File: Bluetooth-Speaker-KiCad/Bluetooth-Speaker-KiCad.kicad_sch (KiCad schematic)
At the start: 0 parts

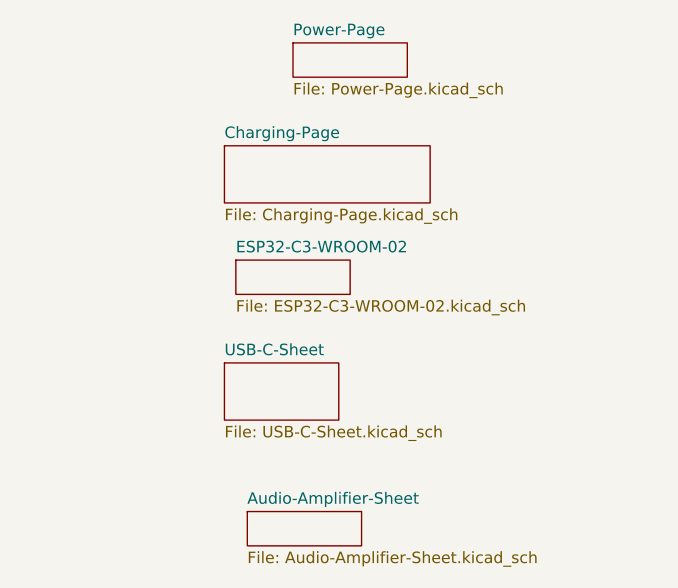
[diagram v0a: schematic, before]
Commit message: USB Connections
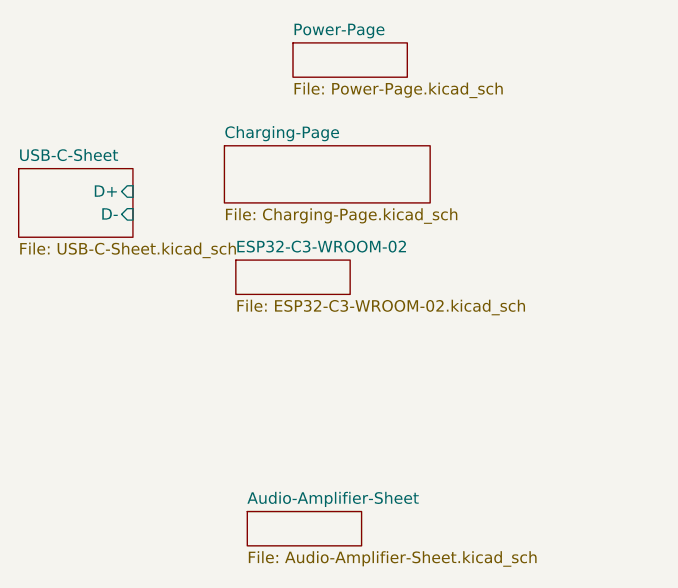
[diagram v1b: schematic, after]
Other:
- sheet USB-C-Sheet ports: added D+, D-; removed none
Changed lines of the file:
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@@
 	)
 	(sheet
-		(at 60.96 72.39)
-		(size 12.7 6.35)
+		(at 38.1 50.8)
+		(size 12.7 7.62)
 		(fields_autoplaced yes)
 		(stroke
@@
 		)
 		(property "Sheetname" "USB-C-Sheet"
-			(at 60.96 71.6784 0)
+			(at 38.1 50.0884 0)
 			(effects
 				(font
@@
 		)
 		(property "Sheetfile" "USB-C-Sheet.kicad_sch"
-			(at 60.96 79.3246 0)
+			(at 38.1 59.0046 0)
 			(effects
 				(font
@@
 			)
 		)
+		(pin "D-" input
+			(at 50.8 55.88 0)
+			(effects
+				(font
+					(size 1.27 1.27)
+				)
+				(justify right)
+			)
+		)
+		(pin "D+" input
+			(at 50.8 53.34 0)
+			(effects
+				(font
+					(size 1.27 1.27)
+				)
+				(justify right)
+			)
+		)

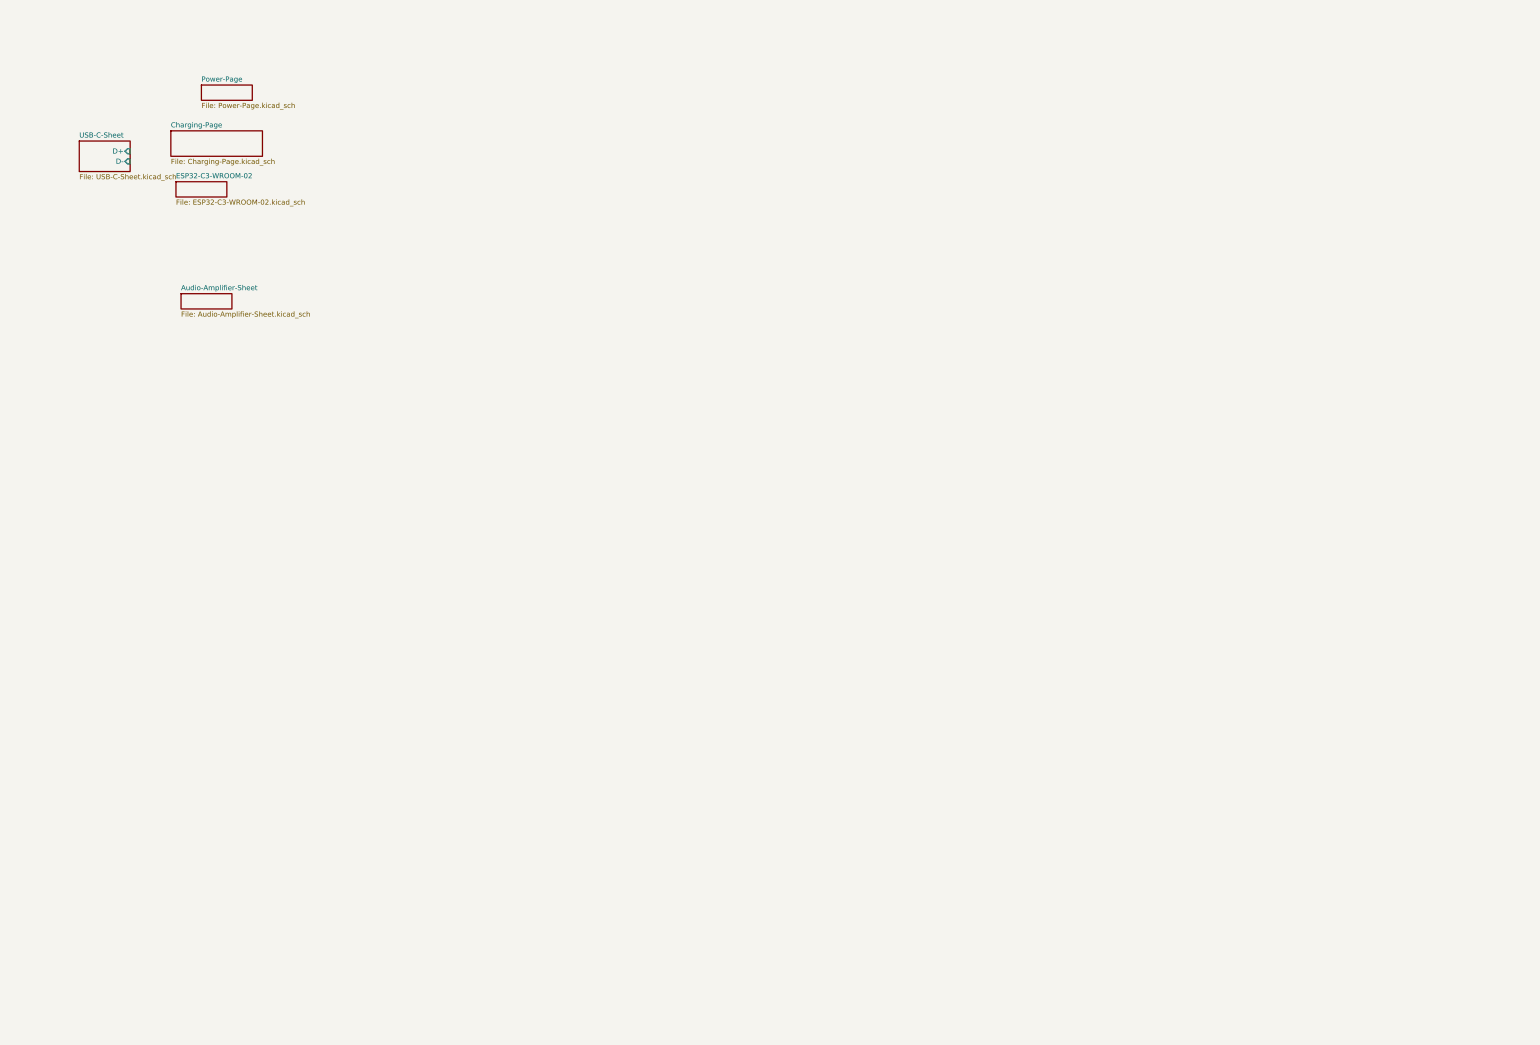
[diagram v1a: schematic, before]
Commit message: Updated battery charging
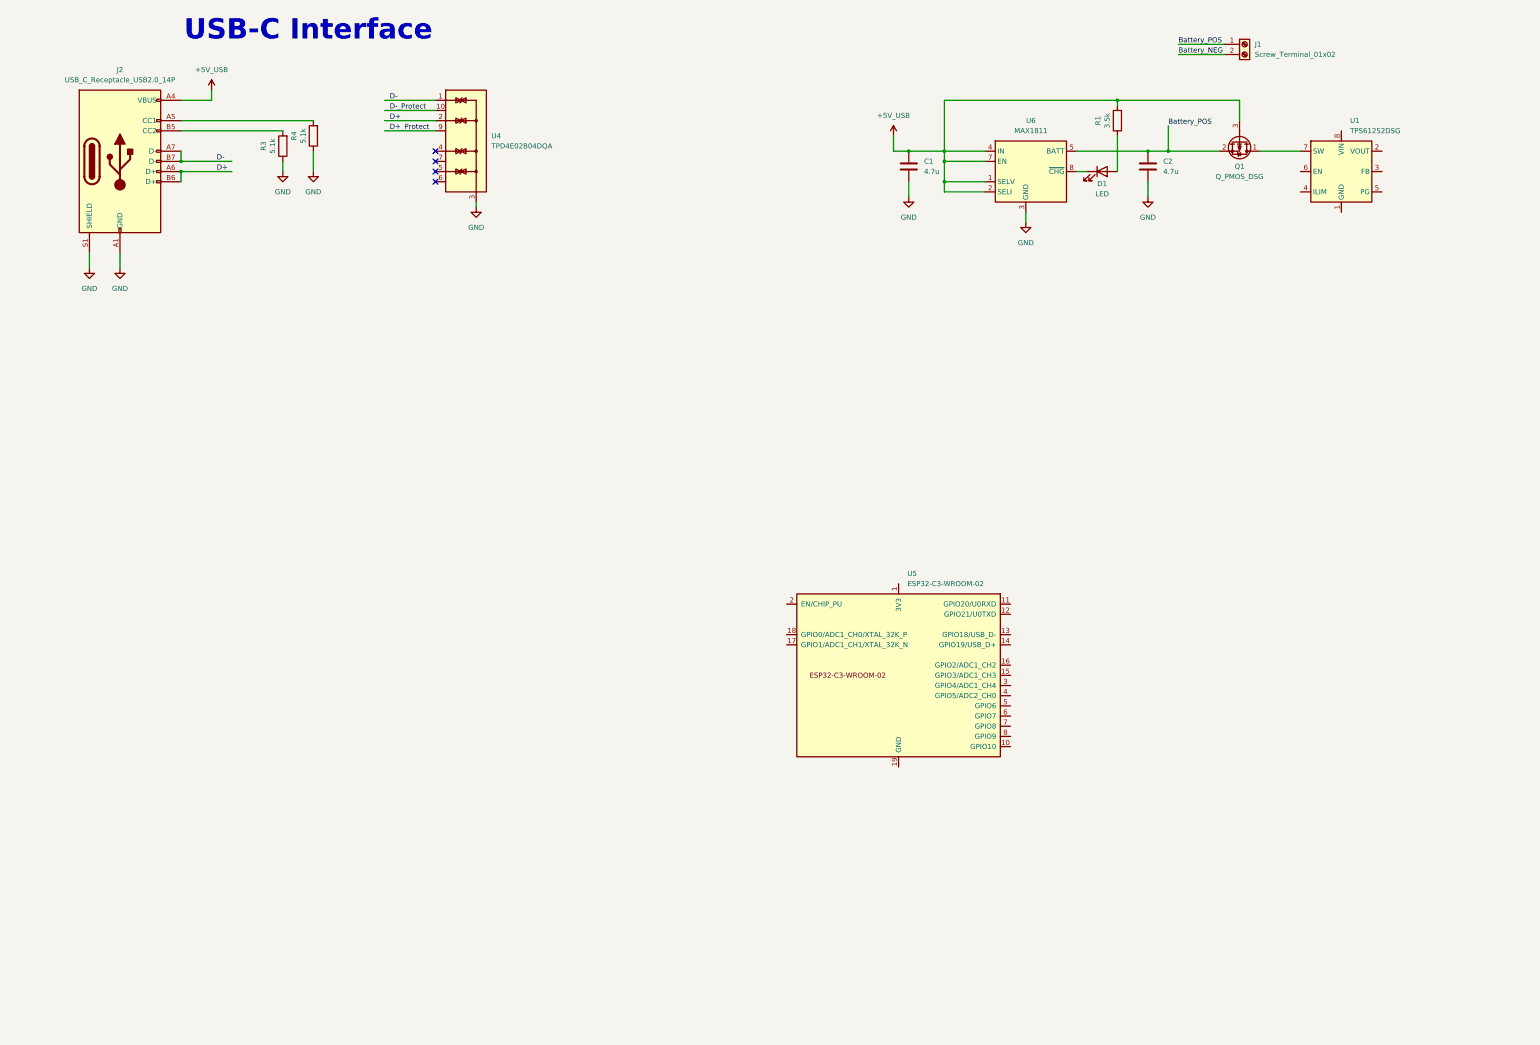
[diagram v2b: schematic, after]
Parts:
- added C1, C2: 4.7u, Capacitor_SMD:C_0603_1608Metric_Pad1.08x0.95mm_HandSolder, symbol Device:C
- added D1: LED, LED_SMD:LED_0603_1608Metric_Pad1.05x0.95mm_HandSolder, symbol Device:LED
- added J1: Screw_Terminal_01x02, symbol Connector:Screw_Terminal_01x02
- added J2: USB_C_Receptacle_USB2.0_14P, symbol Connector:USB_C_Receptacle_USB2.0_14P
- added Q1: Q_PMOS_DSG, symbol Device:Q_PMOS_DSG
- added R1: 3.5k, Resistor_SMD:R_0603_1608Metric_Pad0.98x0.95mm_HandSolder, symbol Device:R
- added R3, R4: 5.1k, Resistor_SMD:R_0603_1608Metric_Pad0.98x0.95mm_HandSolder, symbol Device:R
- added U1: TPS61252DSG, Package_SON:WSON-8-1EP_2x2mm_P0.5mm_EP0.9x1.6mm, symbol Regulator_Switching:TPS61252DSG
- added U4: TPD4E02B04DQA, Package_SON:USON-10_2.5x1.0mm_P0.5mm, symbol Power_Protection:TPD4E02B04DQA
- added U5: ESP32-C3-WROOM-02, PCM_Espressif:ESP32-C3-WROOM-02, symbol PCM_Espressif:ESP32-C3-WROOM-02
- added U6: MAX1811, Package_SO:SOIC-8_3.9x4.9mm_P1.27mm, symbol Battery_Management:MAX1811
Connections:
- new net: D1.1 (K), U6.8 (~{CHG})
- new net: J2.A5 (CC1), R4.2
- new net: U1.1 (GND), U1.9 (GND)
- new net: Q1.1 (D), U1.7 (SW)
- new net: D1.2 (A), R1.1
- new net: J2.B5 (CC2), R3.2
- new net: U5.19 (GND), U5.9 (GND)
- new net +5V_USB: C1.1, J2.A4 (VBUS), J2.A9 (VBUS), J2.B4 (VBUS), J2.B9 (VBUS), Q1.3 (G), R1.2, U6.1 (SELV), U6.2 (SELI), U6.4 (IN), U6.7 (EN)
- new net Battery_NEG: J1.2 (Pin_2)
- new net Battery_POS: C2.1, J1.1 (Pin_1), Q1.2 (S), U6.5 (BATT)
- new net D+: J2.A6 (D+), J2.B6 (D+), U4.2 (IO2)
- new net D+_Protect: U4.9 (NC)
- new net D-: J2.A7 (D-), J2.B7 (D-), U4.1 (IO1)
- new net D-_Protect: U4.10 (NC)
- new net GND: C1.2, C2.2, J2.A1 (GND), J2.A12 (GND), J2.B1 (GND), J2.B12 (GND), J2.S1 (SHIELD), R3.1, R4.1, U4.3 (G), U4.8 (G), U6.3 (GND), U6.6 (GND)
- no-connect marks 0 -> 4
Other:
- removed sheet Audio-Amplifier-Sheet
- removed sheet Charging-Page
- removed sheet ESP32-C3-WROOM-02
- removed sheet Power-Page
- removed sheet USB-C-Sheet
- note added: "USB-C Interface"

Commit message: Updated schematics
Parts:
- removed U1: TPS61252DSG, Package_SON:WSON-8-1EP_2x2mm_P0.5mm_EP0.9x1.6mm, symbol Regulator_Switching:TPS61252DSG
- added C3, C4: 47u, Capacitor_SMD:C_0603_1608Metric_Pad1.08x0.95mm_HandSolder, symbol Device:C
- added C5: 0.1u, Capacitor_SMD:C_0603_1608Metric_Pad1.08x0.95mm_HandSolder, symbol Device:C
- added C6: 10u, Capacitor_SMD:C_0603_1608Metric_Pad1.08x0.95mm_HandSolder, symbol Device:C
- added C7: 1u, Capacitor_SMD:C_0603_1608Metric_Pad1.08x0.95mm_HandSolder, symbol Device:C
- added D2: D_Schottky, Diode_SMD:D_0603_1608Metric_Pad1.05x0.95mm_HandSolder, symbol Device:D_Schottky
- added D3: LED, LED_SMD:LED_0603_1608Metric_Pad1.05x0.95mm_HandSolder, symbol Device:LED
- added L1: 2.2u, Inductor_SMD:L_0805_2012Metric_Pad1.05x1.20mm_HandSolder, symbol Device:L_Ferrite
- added R2, R5, R6: 10k, Resistor_SMD:R_0603_1608Metric_Pad0.98x0.95mm_HandSolder, symbol Device:R
- added R7: 150, Resistor_SMD:R_0603_1608Metric_Pad0.98x0.95mm_HandSolder, symbol Device:R
- added SW1, SW2: SW_Push, symbol Switch:SW_Push
- added U1: RT6150B-33GQW, RT6150B-33GQW:SON50P250X250X80-11N, symbol RT6150B-33GQW:RT6150B-33GQW
- added U2: MAX98357A, Package_DFN_QFN:TQFN-16-1EP_3x3mm_P0.5mm_EP1.23x1.23mm, symbol Audio:MAX98357A
- R1: value 3.5k -> 400
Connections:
- net +5V_USB: now also D2.2 (A)
- net D+_Protect: now also U5.14 (GPIO19/USB_D+)
- net D-_Protect: now also U5.13 (GPIO18/USB_D-)
- net GND: now also U5.19 (GND), U5.9 (GND), C3.2, C4.2, C5.2, C6.2, C7.2, D3.1 (K), SW1.1, SW2.1, U1.11 (EXP), U1.3 (GND), U1.9 (GND__1)
- net at Q1.1 (D): now also C3.1, D2.1 (K), U1.5 (VIN), U1.6 (EN), U1.7 (PS), U1.8 (VINA)
- net +3.3V: now reaches U5.1 (3V3)
- net +3.3V: now also C4.1, C5.1, C6.1, R2.2, R5.2, R6.2, R7.2, U1.1 (VOUT), U1.10 (FB)
- net Boot_Strap_2: now reaches U5.16 (GPIO2/ADC1_CH2)
- net Boot_Strap_2: now also R5.1
- net ESP_EN: now reaches U5.2 (EN/CHIP_PU)
- net ESP_EN: now also C7.1, R2.1, SW2.2
- net Boot_Strap_8: now reaches U5.7 (GPIO8)
- net Boot_Strap_8: now also R6.1
- net Boot_Strap_9: now reaches U5.8 (GPIO9)
- net Boot_Strap_9: now also SW1.2
- new net: L1.1, U1.4 (LX1)
- new net: L1.2, U1.2 (LX2)
- new net: D3.2 (A), R7.1
- new net: U2.11 (GND), U2.15 (GND), U2.3 (GND)
- new net: U2.7 (VDD), U2.8 (VDD)
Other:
- moved on the sheet: C1, C2, D1, J1, Q1, R1, U5, U6

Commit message: Updated schematic
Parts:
- added C8: 10u, Capacitor_SMD:C_0603_1608Metric_Pad1.08x0.95mm_HandSolder, symbol Device:C
- added C9: 0.1u, Capacitor_SMD:C_0603_1608Metric_Pad1.08x0.95mm_HandSolder, symbol Device:C
- added J3: Screw_Terminal_01x02, symbol Connector:Screw_Terminal_01x02
- added R8: 634k, Resistor_SMD:R_0603_1608Metric_Pad0.98x0.95mm_HandSolder, symbol Device:R
- added R9: 100k, Resistor_SMD:R_0603_1608Metric_Pad0.98x0.95mm_HandSolder, symbol Device:R
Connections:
- net +3.3V: now also R8.2
- net Battery_POS: now also U2.7 (VDD), U2.8 (VDD), C8.1, C9.1
- net GND: now also U2.11 (GND), U2.15 (GND), U2.17 (PAD), U2.2 (GAIN_SLOT), U2.3 (GND), C8.2, C9.2, R9.1
- net I2S_BCLK: now reaches U5.3 (GPIO4/ADC1_CH4)
- net I2S_BCLK: now also U2.16 (BCLK)
- net I2S_LRCLK: now reaches U5.4 (GPIO5/ADC2_CH0)
- net I2S_LRCLK: now also U2.14 (LRCLK)
- net I2S_DIN: now reaches U5.5 (GPIO6)
- net I2S_DIN: now also U2.1 (DIN)
- net SD_MODE: now reaches U5.6 (GPIO7)
- net SD_MODE: now also U2.4 (~{SD_MODE}), R8.1, R9.2
- net Speaker_NEG: now reaches U2.10 (OUTN)
- net Speaker_NEG: now also J3.2 (Pin_2)
- net Speaker_POS: now reaches U2.9 (OUTP)
- net Speaker_POS: now also J3.1 (Pin_1)
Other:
- note added: "Audio Amplifier"
- note added: "Battery Charger"
- note added: "Battery Terminal"
- note added: "Buck/Boost Converter"
- note added: "ESP32 C3 Wroom 02"
- moved on the sheet: C1, C2, C3, C4, C5, C6, C7, D1, D2, D3, J1, J2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

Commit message: Updated schematics
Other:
- note added: "ESD Protection"
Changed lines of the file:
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@@
+	)
+	(rectangle
+		(start 113.03 41.91)
+		(end 157.48 88.9)
+		(stroke
+			(width 0)
+			(type solid)
+		)
+		(fill
+			(type none)
+		)
 	)
 	(rectangle
@@
 	(rectangle
 		(start 234.95 113.03)
-		(end 365.76 198.12)
+		(end 365.76 217.17)
 		(stroke
 			(width 0)
@@
 	(text "USB-C Interface"
 		(exclude_from_sim no)
-		(at 95.25 37.084 0)
+		(at 95.25 35.052 0)
 		(effects
 			(font
@@
 			)
 		)
+	)
+	(text "ESD Protection"
+		(exclude_from_sim no)
+		(at 136.144 49.276 0)
+		(effects
+			(font
+				(size 2.54 2.54)
+				(thickness 0.3175)
+			)
+		)
